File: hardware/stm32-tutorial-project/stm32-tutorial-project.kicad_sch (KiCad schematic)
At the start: 0 parts

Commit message: added stm32g4 to schmatic
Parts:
- added U1: STM32G431CBTx, Package_QFP:LQFP-48_7x7mm_P0.5mm, symbol MCU_ST_STM32G4:STM32G431CBTx
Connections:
- new net: U1.23 (VSS), U1.35 (VSS), U1.47 (VSS)
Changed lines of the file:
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@@
 		(comment 2 "designers:")
+	)
+	(symbol
+		(lib_id "MCU_ST_STM32G4:STM32G431CBTx")
+		(at 114.3 101.6 0)
+		(unit 1)
+		(exclude_from_sim no)
+		(in_bom yes)
+		(on_board yes)
+		(dnp no)
+		(fields_autoplaced yes)
+		(property "Reference" "U1"
+			(at 119.0341 139.065 0)
+			(effects
+				(font
+					(size 1.27 1.27)
+				)
+				(justify left)
+			)
+		)
+		(property "Value" "STM32G431CBTx"
+			(at 119.0341 141.605 0)
+			(effects
+				(font
+					(size 1.27 1.27)
+				)
+				(justify left)
+			)
+		)
+		(property "Footprint" "Package_QFP:LQFP-48_7x7mm_P0.5mm"
+			(at 101.6 137.16 0)
+			(effects
+				(font
+					(size 1.27 1.27)
+				)
+				(justify right)
+				(hide yes)
+			)
+		)
+		(property "Datasheet" "https://www.st.com/resource/en/datasheet/stm32g431cb.pdf"
+			(at 114.3 101.6 0)
+			(effects
+				(font
+					(size 1.27 1.27)
+				)
+				(hide yes)
+			)
+		)
+		(property "Description" "STMicroelectronics Arm Cortex-M4 MCU, 128KB flash, 32KB RAM, 170 MHz, 1.71-3.6V, 38 GPIO, LQFP48"
+			(at 114.3 101.6 0)
+			(effects
+				(font
+					(size 1.27 1.27)
+				)
+				(hide yes)
+			)
+		)
+		(pin "24"
+		)
+		(pin "15"
+		)
+		(pin "7"
+		)
+		(pin "9"
+		)
+		(pin "21"
+		)
+		(pin "4"
+		)
+		(pin "42"
+		)
+		(pin "25"
+		)
+		(pin "31"
+		)
+		(pin "32"
+		)
+		(pin "3"
+		)
+		(pin "45"
+		)
+		(pin "22"
+		)
+		(pin "46"
+		)
+		(pin "28"
+		)
+		(pin "12"
+		)
+		(pin "14"
+		)
+		(pin "10"
+		)
+		(pin "37"
+		)
+		(pin "40"
+		)
+		(pin "27"
+		)
+		(pin "13"
+		)
+		(pin "43"
+		)
+		(pin "47"
+		)
+		(pin "26"
+		)
+		(pin "23"
+		)
+		(pin "29"
+		)
+		(pin "19"
+		)
+		(pin "1"
+		)
+		(pin "17"
+		)
+		(pin "11"
+		)
+		(pin "34"
+		)
+		(pin "18"
+		)
+		(pin "30"
+		)
+		(pin "35"
+		)
+		(pin "36"
+		)
+		(pin "38"
+		)
+		(pin "33"
+		)
+		(pin "39"
+		)
+		(pin "41"
+		)
+		(pin "16"
+		)
+		(pin "2"
+		)
+		(pin "44"
+		)
+		(pin "20"
+		)
+		(pin "5"
+		)
+		(pin "48"
+		)
+		(pin "6"
+		)
+		(pin "8"
+		)
+		(instances
+			(project "stm32-tutorial-project"
+				(path "/d669673b-e709-4a82-ac8c-4eb3d8c60d0b"
+					(reference "U1")
+					(unit 1)
+				)
+			)
+		)
 	)
 	(sheet_instances

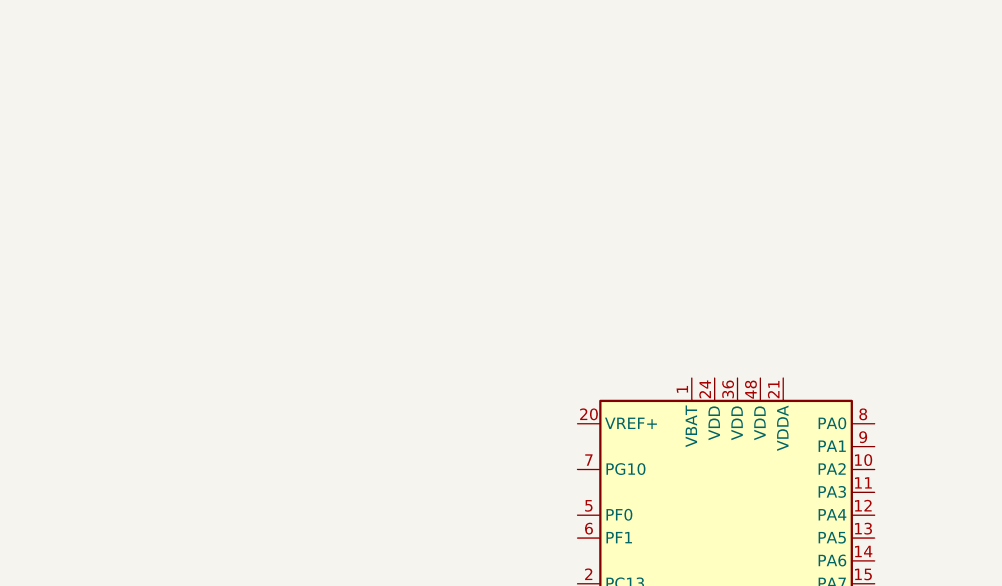
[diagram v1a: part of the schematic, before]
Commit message: added decoupling caps to mcu
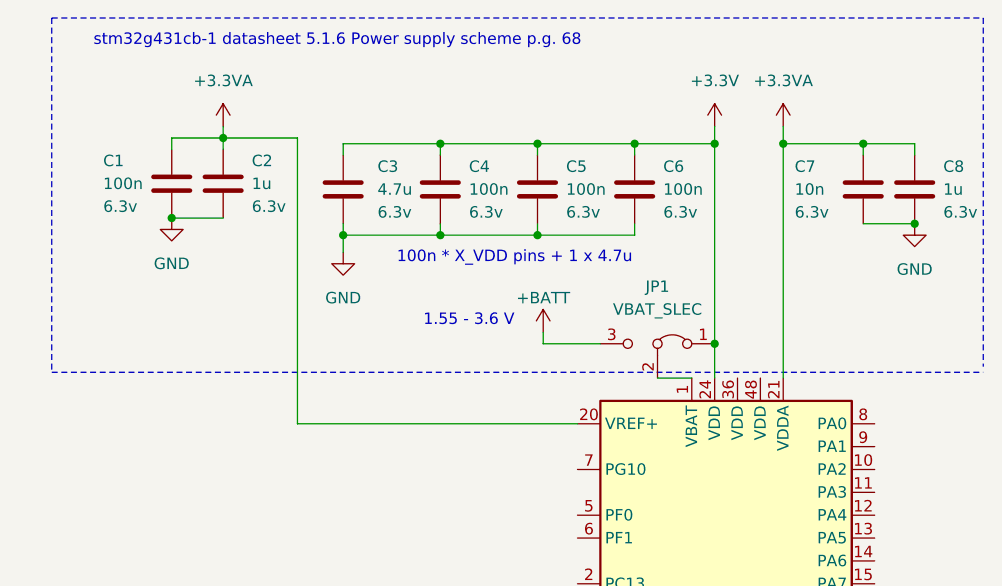
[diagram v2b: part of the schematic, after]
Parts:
- added C1, C4, C5, C6: 100n, symbol Device:C
- added C2, C8: 1u, symbol Device:C
- added C3: 4.7u, symbol Device:C
- added C7: 10n, symbol Device:C
- added JP1: VBAT_SLEC, symbol Jumper:Jumper_3_Bridged12
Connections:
- net at U1.1 (VBAT): now also JP1.2 (C)
- net +3.3VA: now reaches U1.20 (VREF+)
- net +3.3VA: now also U1.21 (VDDA), C1.1, C2.1, C7.1, C8.1
- net +3.3V: now reaches U1.24 (VDD)
- net +3.3V: now also C3.1, C4.1, C5.1, C6.1, JP1.1 (A)
- new net +BATT: JP1.3 (B)
- new net GND: C1.2, C2.2, C3.2, C4.2, C5.2, C6.2, C7.2, C8.2
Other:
- note added: "1.55 - 3.6 V"
- note added: "100n * X_VDD pins + 1 x 4.7u"
- note added: "stm32g431cb-1 datasheet 5.1.6 Power supply scheme p.g. 68"

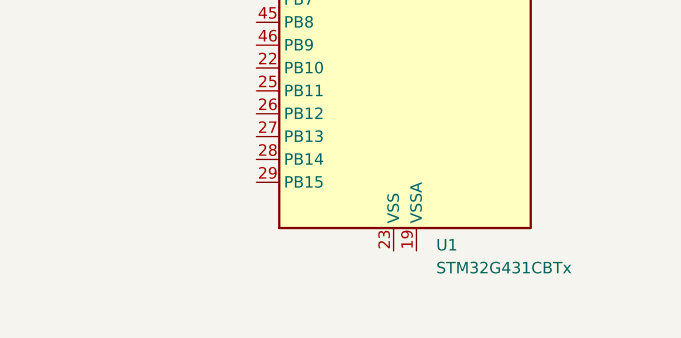
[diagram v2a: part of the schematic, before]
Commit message: added decoupling caps to mcu
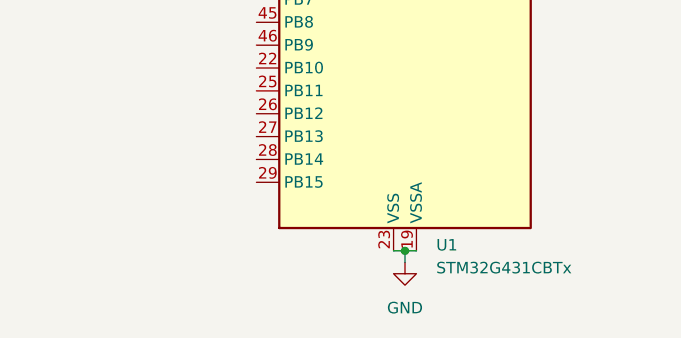
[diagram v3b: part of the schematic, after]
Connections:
- net GND: now also U1.19 (VSSA), U1.23 (VSS), U1.35 (VSS), U1.47 (VSS)
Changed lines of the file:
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@@
+	)
+	(junction
+		(at 115.57 139.7)
+		(diameter 0)
+		(color 0 0 0 0)
 	)
 	(junction
@@
 	(wire
 		(pts
+			(xy 115.57 139.7) (xy 116.84 139.7)
+		)
+		(stroke
+			(width 0)
+			(type default)
+		)
+	)
+	(wire
+		(pts
 			(xy 73.025 43.815) (xy 73.025 45.085)
 		)
@@
 	(wire
 		(pts
+			(xy 115.57 139.7) (xy 115.57 140.97)
+		)
+		(stroke
+			(width 0)
+			(type default)
+		)
+	)
+	(wire
+		(pts
 			(xy 114.3 33.02) (xy 114.3 34.925)
 		)
@@
 		(pts
 			(xy 53.975 43.18) (xy 59.69 43.18)
+		)
+		(stroke
+			(width 0)
+			(type default)
+		)
+	)
+	(wire
+		(pts
+			(xy 114.3 139.7) (xy 115.57 139.7)
 		)
 		(stroke
@@
 					(unit 1)
 				)
+			)
+		)
+	)
+	(symbol
+		(lib_id "power:GND")
+		(at 115.57 140.97 0)
+		(unit 1)
+		(exclude_from_sim no)
+		(in_bom yes)
+		(on_board yes)
+		(dnp no)
+		(fields_autoplaced yes)
+		(property "Reference" "#PWR08"
+			(at 115.57 147.32 0)
+			(effects
+				(font
+					(size 1.27 1.27)
+				)
+				(hide yes)
+			)
+		)
+		(property "Value" "GND"
+			(at 115.57 146.05 0)
+			(effects
+				(font
+					(size 1.27 1.27)
+				)
+			)
+		)
+		(property "Footprint" ""
+			(at 115.57 140.97 0)
+			(effects
+				(font
+					(size 1.27 1.27)
+				)
+				(hide yes)
+			)
+		)
+		(property "Datasheet" ""
+			(at 115.57 140.97 0)
+			(effects
+				(font
+					(size 1.27 1.27)
+				)
+				(hide yes)
+			)
+		)
+		(property "Description" "Power symbol creates a global label with name \"GND\" , ground"
+			(at 115.57 140.97 0)
+			(effects
+				(font
+					(size 1.27 1.27)
+				)
+				(hide yes)
+			)
+		)
+		(pin "1"
+		)
+		(instances
+			(project "stm32-tutorial-project"
+				(path "/d669673b-e709-4a82-ac8c-4eb3d8c60d0b"
+					(reference "#PWR08")
+					(unit 1)
+				)

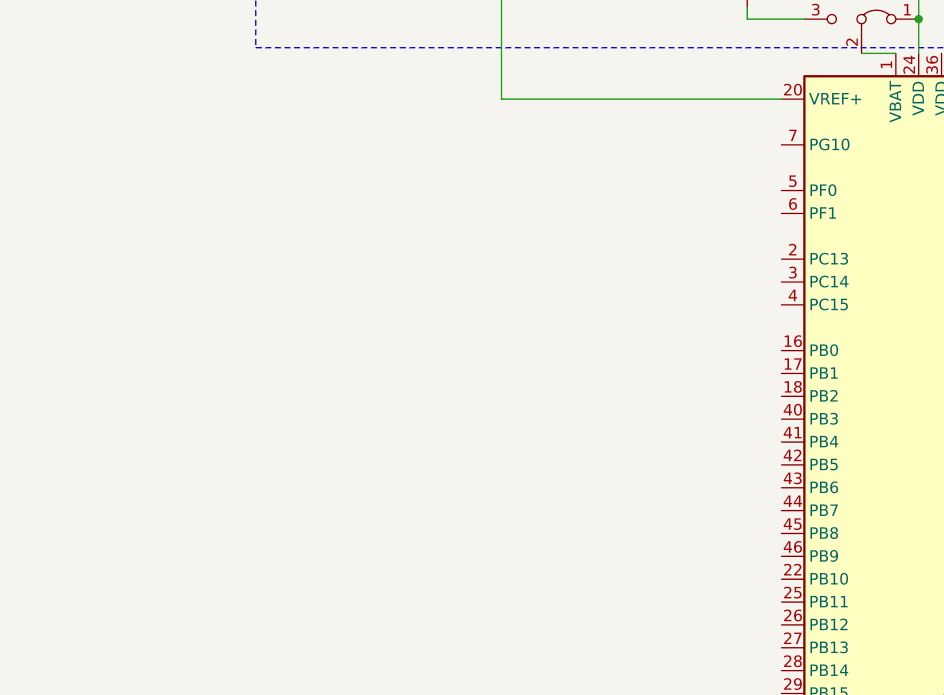
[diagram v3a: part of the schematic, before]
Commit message: added crystal to schmatic
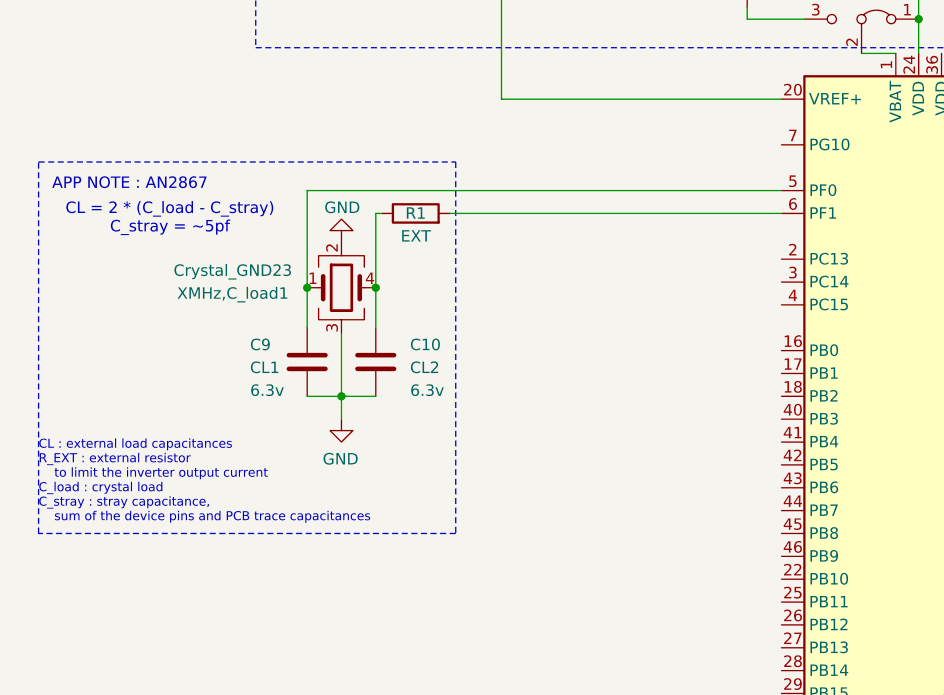
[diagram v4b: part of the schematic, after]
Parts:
- added C10: CL2, symbol Device:C
- added C9: CL1, symbol Device:C
- added R1: EXT, symbol Device:R
- added XMHz,C_load1: Crystal_GND23, symbol Device:Crystal_GND23
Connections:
- net GND: now also C10.2, C9.2, XMHz,C_load1.2, XMHz,C_load1.3
- net at U1.5 (PF0): now also C9.1, XMHz,C_load1.1
- net at U1.6 (PF1): now also R1.2
- new net: C10.1, R1.1, XMHz,C_load1.4
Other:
- note added: "APP NOTE : AN2867"
- note added: "CL : external load capacitances R_EXT : external resistor to limit the inverter output current C_load : crystal load C_stray : stray capacitance, sum of the device pins and PCB trace capacitances"
- note added: "CL = 2 * (C_load - C_stray) C_stray = ~5pf"

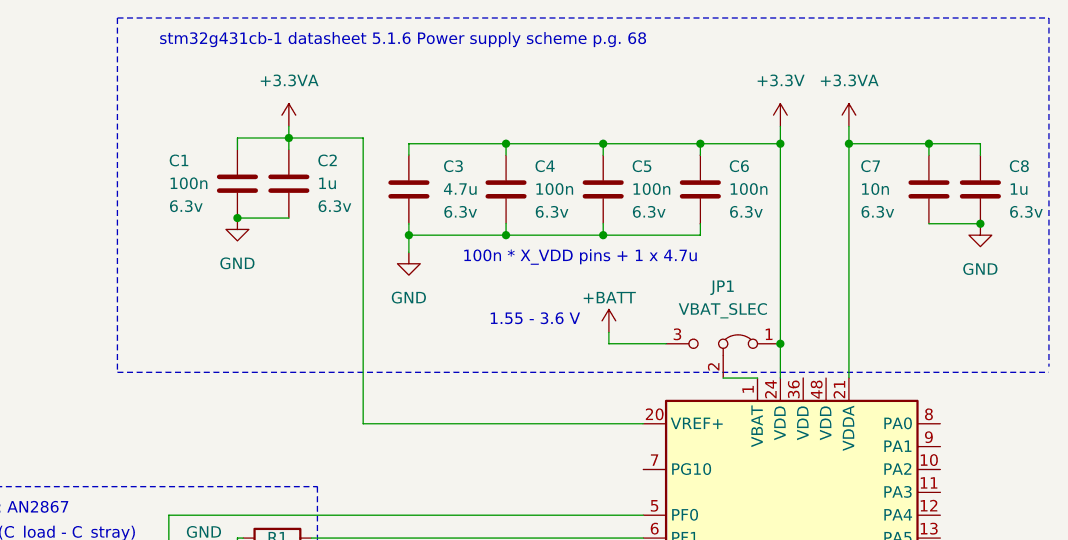
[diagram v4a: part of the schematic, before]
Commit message: added ferrite beads to analog power
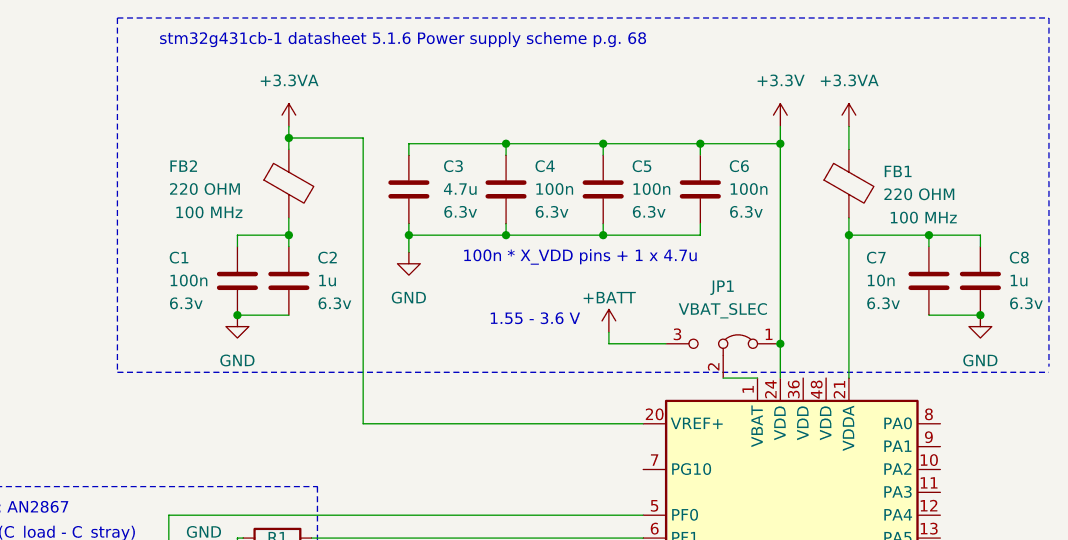
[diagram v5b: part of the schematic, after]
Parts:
- added FB1, FB2: 220 OHM, Inductor_SMD:L_0603_1608Metric_Pad1.05x0.95mm_HandSolder, symbol Device:FerriteBead
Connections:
- net +3.3VA: now also FB1.1, FB2.1; no longer C1.1, C2.1, C7.1, C8.1, U1.21 (VDDA)
- new net: C7.1, C8.1, FB1.2, U1.21 (VDDA)
- new net: C1.1, C2.1, FB2.2
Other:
- moved on the sheet: C1, C2, C7, C8

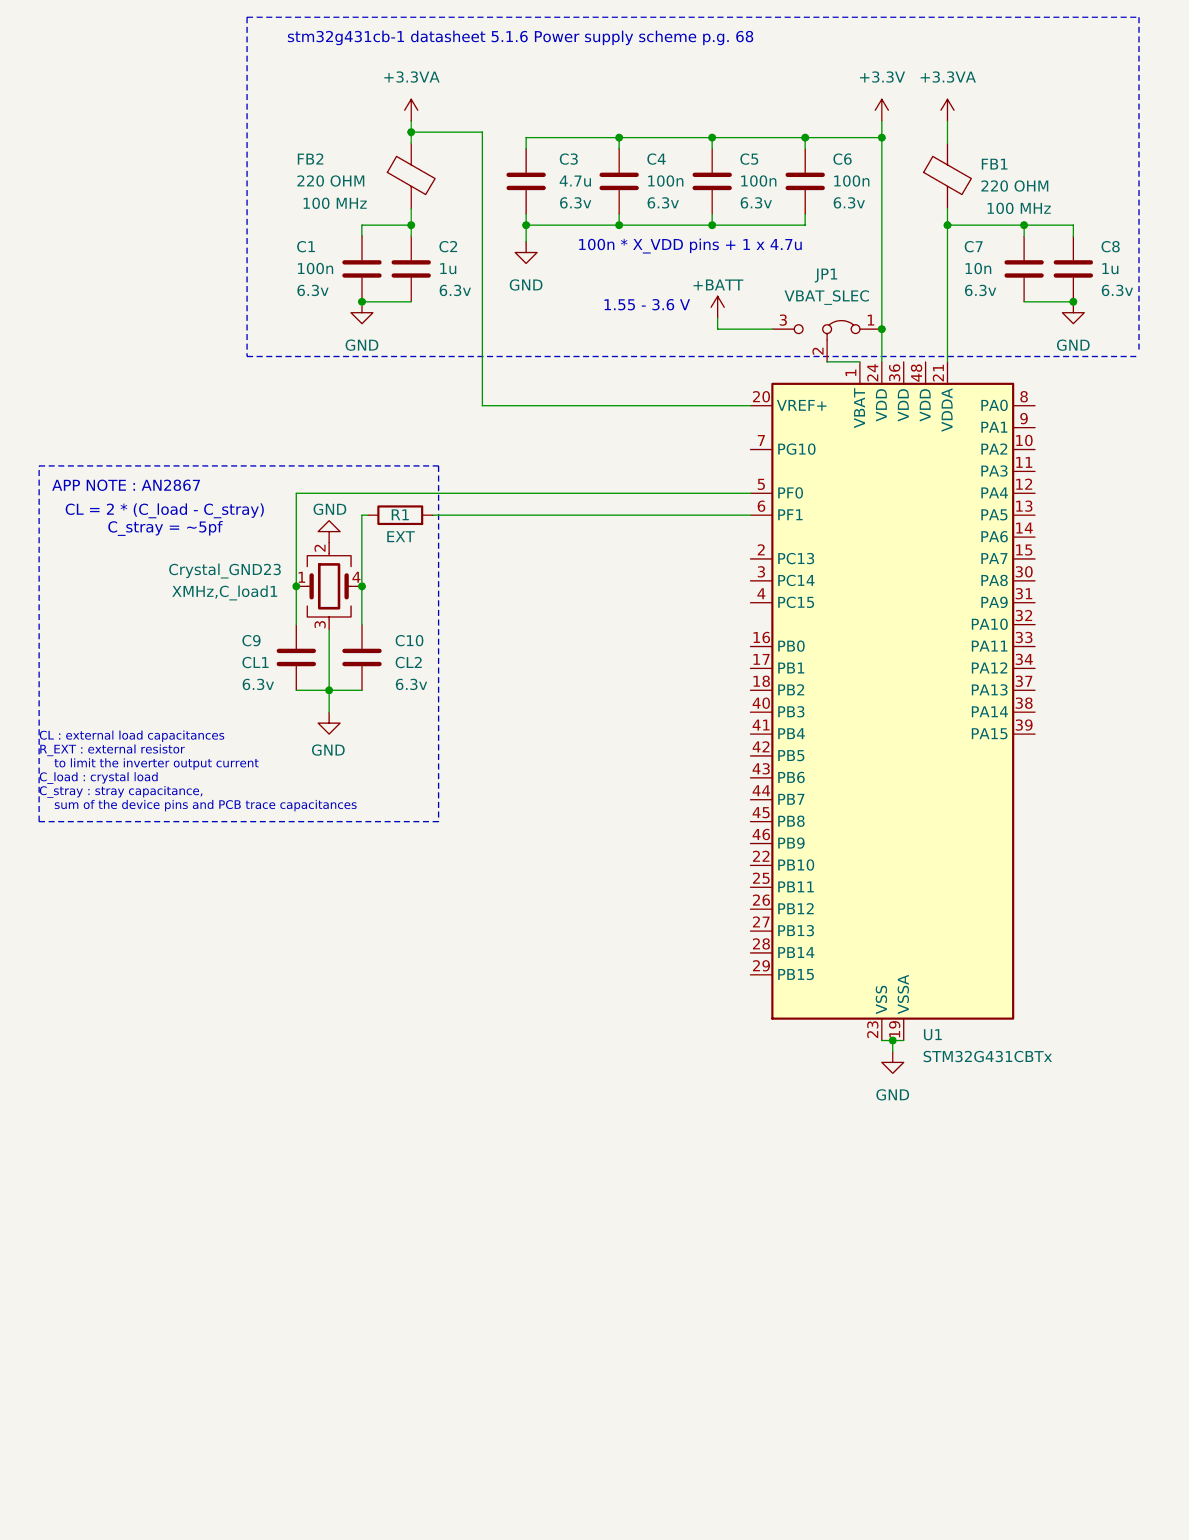
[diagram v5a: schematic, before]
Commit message: added reset button
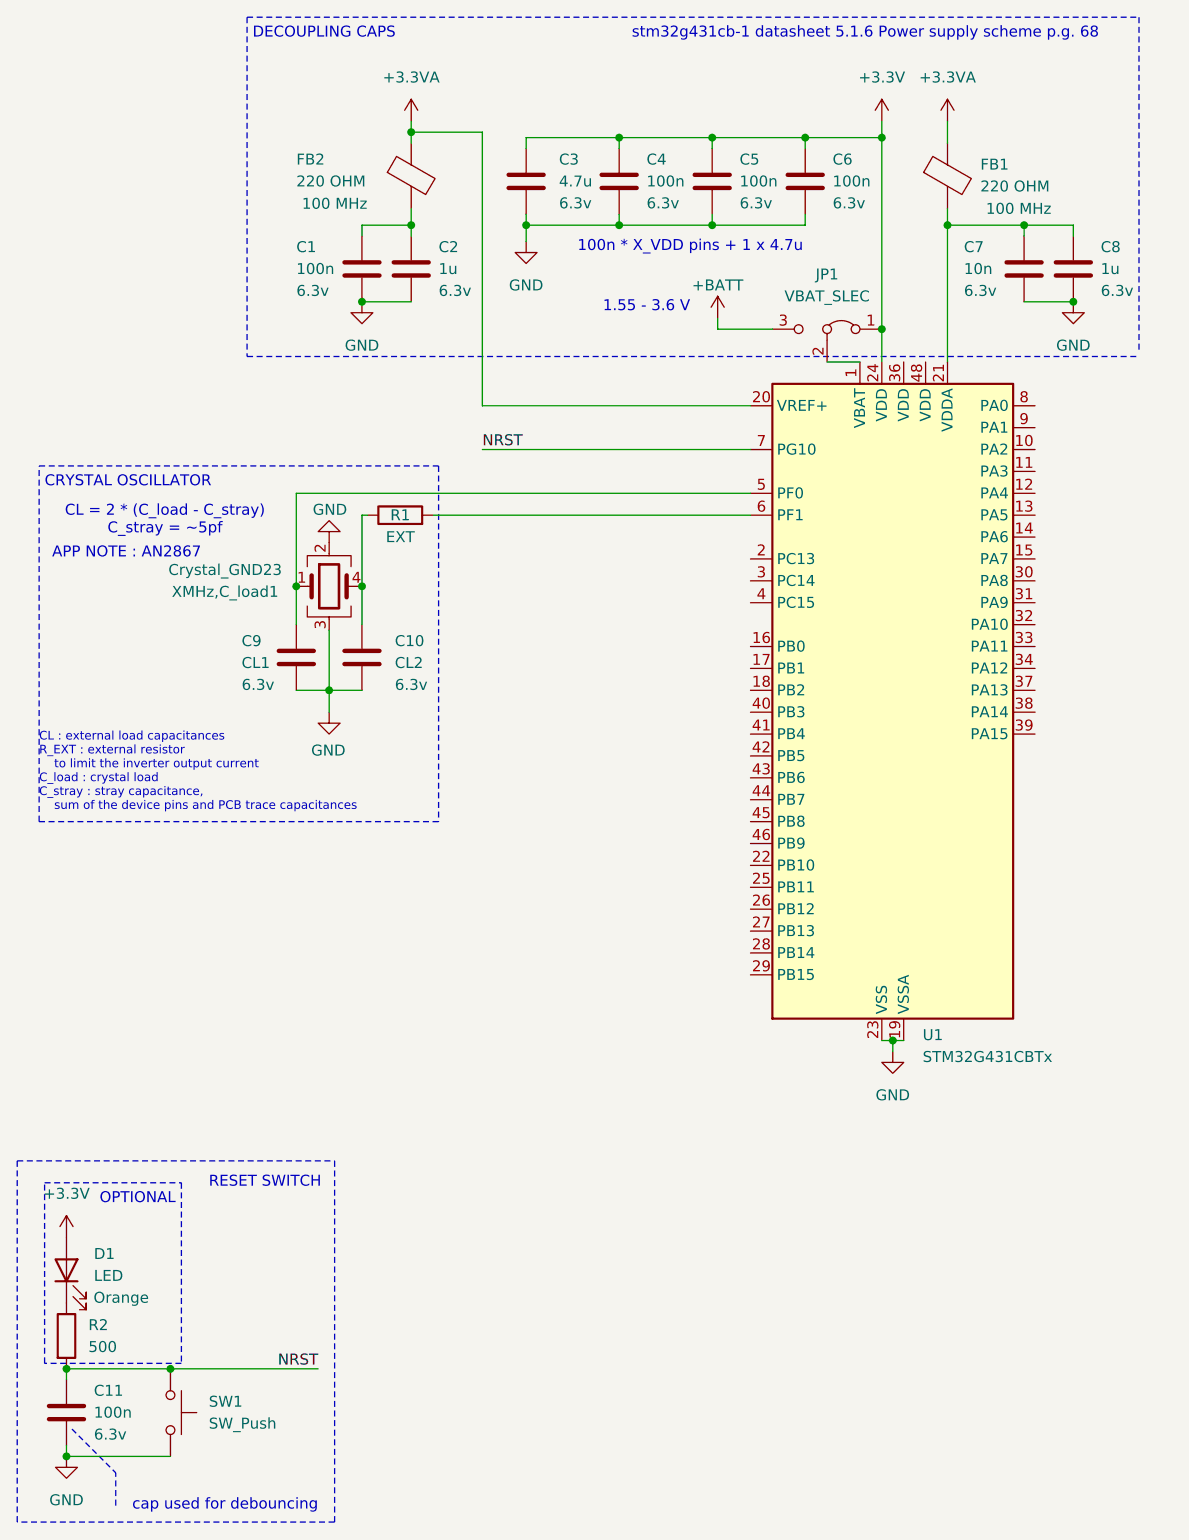
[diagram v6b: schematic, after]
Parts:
- added C11: 100n, symbol Device:C
- added D1: LED, symbol Device:LED
- added R2: 500, symbol Device:R
- added SW1: SW_Push, symbol Switch:SW_Push
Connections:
- net +3.3V: now also D1.2 (A)
- net GND: now also C11.2, SW1.2
- net NRST: now reaches U1.7 (PG10)
- net NRST: now also C11.1, R2.2, SW1.1
- new net: D1.1 (K), R2.1
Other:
- note added: "CRYSTAL OSCILLATOR"
- note added: "DECOUPLING CAPS"
- note added: "OPTIONAL"
- note added: "RESET SWITCH"
- note added: "cap used for debouncing"
